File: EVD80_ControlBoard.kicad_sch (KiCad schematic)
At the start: 92 parts, among them U1 LD1117S12TR_SOT223, U2 R-78E3.3-1.0, U3 R-78E5.0-1.0, U4 TL431, U5 LMV324, U7 TMS320F28379DPTPQ

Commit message: Добавления: Расставил все на плате
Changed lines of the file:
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@@
 	)
 	(global_label "VREFHIC"
-		(shape input)
+		(shape output)
 		(at 129.54 250.19 0)
 		(fields_autoplaced yes)
@@
 		)
 		(property "Intersheetrefs" "${INTERSHEET_REFS}"
-			(at 139.7545 250.1106 0)
+			(at 140.3267 250.19 0)
 			(effects
 				(font
@@
 	)
 	(global_label "VREFHID"
-		(shape input)
+		(shape output)
 		(at 193.04 250.19 0)
 		(fields_autoplaced yes)
@@
 		)
 		(property "Intersheetrefs" "${INTERSHEET_REFS}"
-			(at 203.2545 250.1106 0)
+			(at 203.8267 250.19 0)
 			(effects
 				(font
@@
 	)
 	(global_label "VREFHIA"
-		(shape input)
+		(shape output)
 		(at 191.77 212.09 0)
 		(fields_autoplaced yes)
@@
 		)
 		(property "Intersheetrefs" "${INTERSHEET_REFS}"
-			(at 201.8031 212.0106 0)
+			(at 202.3753 212.09 0)
 			(effects
 				(font
@@
 	)
 	(global_label "VREFHIB"
-		(shape input)
+		(shape output)
 		(at 128.27 212.09 0)
 		(fields_autoplaced yes)
@@
 		)
 		(property "Intersheetrefs" "${INTERSHEET_REFS}"
-			(at 138.4845 212.0106 0)
+			(at 139.0567 212.09 0)
 			(effects
 				(font

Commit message: Изменения: развел все
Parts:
- R5: value 1.5k -> 680
- R6: value 1.5k -> 1k
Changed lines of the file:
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@@
 		(fields_autoplaced yes)
 		(property "Reference" "R6"
-			(at 98.298 98.2253 0)
-			(effects
-				(font
-					(size 1.27 1.27)
-				)
-				(justify left)
-			)
-		)
-		(property "Value" "1.5k"
-			(at 98.298 100.7622 0)
+			(at 99.06 97.7899 0)
+			(effects
+				(font
+					(size 1.27 1.27)
+				)
+				(justify left)
+			)
+		)
+		(property "Value" "1k"
+			(at 99.06 100.3299 0)
 			(effects
 				(font
@@
 		(fields_autoplaced yes)
 		(property "Reference" "R5"
-			(at 98.298 47.4253 0)
-			(effects
-				(font
-					(size 1.27 1.27)
-				)
-				(justify left)
-			)
-		)
-		(property "Value" "1.5k"
-			(at 98.298 49.9622 0)
-			(effects
-				(font
+			(at 99.06 46.9899 0)
+			(effects
+				(font
+					(size 1.27 1.27)
+				)
+				(justify left)
+			)
+		)
+		(property "Value" "680"
+			(at 99.06 49.5299 0)
+			(effects
+				(font

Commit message: REV_C: добавил Э3
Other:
- note added: "НВЦТ.EVP150-2-1.3000.100"
- note added: "Схема электрическая принципиальная"
- company: (none) -> ООО "Электротранспортные технологии"
- title: (none) -> Плата управления
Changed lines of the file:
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@@
 (kicad_sch
-	(version 20231120)
+	(version 20250114)
 	(generator "eeschema")
-	(generator_version "8.0")
+	(generator_version "9.0")
 	(paper "A3")
+	(title_block
+		(title "Плата управления")
+		(company "ООО \"Электротранспортные технологии\"")
+		(comment 1 "НВЦТ.EVP150-2-1.3000.100 Э3")
+		(comment 2 "Филатов А.С.")
+		(comment 3 "Сизякин А.В.")
+		(comment 4 "Коваленко В.А.")
+		(comment 6 "Зубков Д.Н.")
+	)
+	(text "Схема электрическая принципиальная"
+		(exclude_from_sim no)
+		(at 330.708 272.288 0)
+		(effects
+			(font
+				(size 2.5 2.5)
+			)
+		)
+	)
+	(text "1.2V Regulator"
+		(exclude_from_sim no)
+		(at 67.31 133.35 0)
+		(effects
+			(font
+				(size 2.543 2.543)
+			)
+			(justify left bottom)
+		)
+	)
+	(text "3.3V Regulator"
+		(exclude_from_sim no)
+		(at 59.69 31.75 0)
+		(effects
+			(font
+				(size 2.543 2.543)
+			)
+			(justify left bottom)
+		)
+	)
+	(text "НВЦТ.EVP150-2-1.3000.100"
+		(exclude_from_sim no)
+		(at 16.51 35.306 90)
+		(effects
+			(font
+				(size 2.5 2.5)
+			)
+		)
+	)
+	(text "5V Regulator"
+		(exclude_from_sim no)
+		(at 59.69 82.55 0)
+		(effects
+			(font
+				(size 2.543 2.543)
+			)
+			(justify left bottom)
+		)
+	)
+	(text "ADC Reference"
+		(exclude_from_sim no)
+		(at 73.66 190.5 0)
+		(effects
+			(font
+				(size 2.543 2.543)
+			)
+			(justify left bottom)
+		)
+	)
+	(text "Hierarchical Sheets"
+		(exclude_from_sim no)
+		(at 490.22 15.24 0)
+		(effects
+			(font
+				(size 5.08 5.08)
+			)
+			(justify left bottom)
+		)
+	)
 	(junction
 		(at 368.3 81.28)
@@
 		)
 	)
-	(text "1.2V Regulator"
-		(exclude_from_sim no)
-		(at 67.31 133.35 0)
-		(effects
-			(font
-				(size 2.543 2.543)
-			)
-			(justify left bottom)
-		)
-	)
-	(text "3.3V Regulator"
-		(exclude_from_sim no)
-		(at 59.69 31.75 0)
-		(effects
-			(font
-				(size 2.543 2.543)
-			)
-			(justify left bottom)
-		)
-	)
-	(text "5V Regulator"
-		(exclude_from_sim no)
-		(at 59.69 82.55 0)
-		(effects
-			(font
-				(size 2.543 2.543)
-			)
-			(justify left bottom)
-		)
-	)
-	(text "ADC Reference"
-		(exclude_from_sim no)
-		(at 73.66 190.5 0)
-		(effects
-			(font
-				(size 2.543 2.543)
-			)
-			(justify left bottom)
-		)
-	)
-	(text "Hierarchical Sheets"
-		(exclude_from_sim no)
-		(at 490.22 15.24 0)
-		(effects
-			(font
-				(size 5.08 5.08)
-			)
-			(justify left bottom)
-		)
-	)
 	(global_label "VREFHIC"
 		(shape output)
@@
 		(at 508 177.8)
 		(size 36.83 25.4)
+		(exclude_from_sim no)
+		(in_bom yes)
+		(on_board yes)
+		(dnp no)
 		(stroke
 			(width 0.1524)
@@
 		(at 558.8 25.4)
 		(size 38.1 25.4)
+		(exclude_from_sim no)
+		(in_bom yes)
+		(on_board yes)
+		(dnp no)
 		(stroke
 			(width 0.1524)
@@
 		(at 558.8 177.8)
 		(size 38.1 25.4)
+		(exclude_from_sim no)
+		(in_bom yes)
+		(on_board yes)
+		(dnp no)
 		(stroke
 			(width 0.1524)
@@
 		(at 508 63.5)
 		(size 38.1 25.4)
+		(exclude_from_sim no)
+		(in_bom yes)
+		(on_board yes)
+		(dnp no)
 		(stroke
 			(width 0.1524)
@@
 		(at 508 139.7)
 		(size 38.1 25.4)
+		(exclude_from_sim no)
+		(in_bom yes)
+		(on_board yes)
+		(dnp no)
 		(stroke
 			(width 0.1524)
@@
 		(at 457.2 25.4)
 		(size 38.1 25.4)
+		(exclude_from_sim no)
+		(in_bom yes)
+		(on_board yes)
+		(dnp no)
 		(stroke
 			(width 0.1524)
@@
 		(at 457.2 177.8)
 		(size 38.1 25.4)
+		(exclude_from_sim no)
+		(in_bom yes)
+		(on_board yes)
+		(dnp no)
 		(stroke
 			(width 0.1524)
@@
 		(at 558.8 101.6)
 		(size 38.1 25.4)
+		(exclude_from_sim no)
+		(in_bom yes)
+		(on_board yes)
+		(dnp no)
 		(stroke
 			(width 0.1524)
@@
 		(at 457.2 139.7)
 		(size 38.1 25.4)
+		(exclude_from_sim no)
+		(in_bom yes)
+		(on_board yes)
+		(dnp no)
 		(stroke
 			(width 0.1524)
@@
 		(at 508 101.6)
 		(size 38.1 25.4)
+		(exclude_from_sim no)
+		(in_bom yes)
+		(on_board yes)
+		(dnp no)
 		(stroke
 			(width 0.1524)
@@
 		(at 457.2 101.6)
 		(size 38.735 25.4)
+		(exclude_from_sim no)
+		(in_bom yes)
+		(on_board yes)
+		(dnp no)
 		(stroke
 			(width 0.1524)
@@
 		(at 508 25.4)
 		(size 38.1 25.4)
+		(exclude_from_sim no)
+		(in_bom yes)
+		(on_board yes)
+		(dnp no)
 		(stroke
 			(width 0.1524)
@@
 		(at 457.2 63.5)
 		(size 38.1 25.4)
+		(exclude_from_sim no)
+		(in_bom yes)
+		(on_board yes)
+		(dnp no)
 		(stroke
 			(width 0.1524)
@@
 		(at 558.8 139.7)
 		(size 38.1 25.4)
+		(exclude_from_sim no)
+		(in_bom yes)
+		(on_board yes)
+		(dnp no)
 		(stroke
 			(width 0.1524)
@@
 		(at 457.2 215.9)
 		(size 38.1 25.4)
+		(exclude_from_sim no)
+		(in_bom yes)
+		(on_board yes)
+		(dnp no)
 		(stroke
 			(width 0.1524)
@@
 		(at 558.8 63.5)
 		(size 38.1 25.4)
+		(exclude_from_sim no)
+		(in_bom yes)
+		(on_board yes)
+		(dnp no)
 		(stroke
 			(width 0.1524)
@@
 		)
 	)
+	(embedded_fonts no)
+	(embedded_files
+		(file
+			(name "gost_landscape.kicad_wks")
+			(type worksheet)
+			(data |KLUv/WC6IO0nAEYqgjFAc9pUwaAq7rGQvf7J+ej28lrFVi+Ra0Qr0XvBpp0PVIKJocju3inLuMxu
+				WJMBZ+8LfABnAHoALNo2GUZx9Wyv+vGO7GqGEQi0h1NBVbQbu4asUlxtNdu0DUOHHXuz3S4LorjC
+				2E01EGgMV8+VUWw3dfNo1moMH81SFXzgYBtVTc4wznZ5FqxD7VTQq7ccP9gGTKJmWIeqoOVcJzCQ
+				DVVL8SfCVhDFDBBgIzTR1VmonOtDBRi2oWoZrJTd7jX9n7Khe3Oye/9Ms1rmYPfHZufeRc3LSf+n
+				jA0dvmaRc3bwZWv+XePfzun8KCGM/7Cfewzne/kzOnz97xpCdtQnfM1OdoRSwyL6ns9/yCEXdTKt
+				OdMw+9FeW47UoQcp1/Kgs+ReeFeQbod89jhy6K+b4b9sl8309ehUweEadu1UTChOpuuy4U1LLpJO
+				lVtSuhJakbPaCV0eintGDej97uhEuhmOcrWX1TbJb5lclmu6pItyMa5v1WZ1wyIHzIIiICx/hlaE
+				zSDtgyDQGGvlWpxSbsstXdJLQQAB1cP21+/uObTaZWza0c22HZYs36ROMpS0m+FjF6MbeD2fZOgw
+				wZ3rg/x/m2kOFM+HkHnw/SDTPLsg89wrZHil5ZLQ0Wmkp4vQlk4KkREFxB1+PPn90ttfe+myyeUD
+				umO5J3flmlwuU5xO7sejFKfRiSWBbahBUahmpCAFSSHDGnGRwBiC1Z0dskgQgjAUw4AcCGIcAhlC
+				HCFEQAwhhBhjREauHS1W9GqoT2ej9oib6AkUZ1xytemsseM0xpmg8F4VpZ0BeQEinRqXR/LHvcXM
+				zxBtuIUaw8HcSNawPE002iKV23H6UV273ntSIAlTA5N1ZdrndCiVe6uBaRiHYYiKq9GgNrTeNTRf
+				NfUJ/32bWh9/57DHw7uQxz4ULHfFeApmWDLvyo3GHRcRbczSKYx08fXGVh6xzSXRvDpB6BApYY8y
+				6sEbrKBGeegRkrjMrCrrLxeLYxp0HswTCskvDBMXTHE/T+ByeqaPP3qdKzND8/1VD3bUDeJn0Y9z
+				gDZPfEvFjAaAJZpbLUtz3kaxhDe3Snk/4OyFwqFNmJyv7iYuCzQrtB3ykyQKiwBJcw2JxNU32g3/
+				kVAxeFgRdQg12uIi1pyRGPpIH4Xa+rlwJouAD+8zrEHs/Mj95yRfSbzxr/d0A4lRg1eZtAqJQBlT
+				3zHGdrqzkPo5zEAHci6R5WaJ7M8aOMeYTH8ylU/JOjqDbeYB3A/SED8iC0uFsZZlGFxjlGVAmFBW
+				Sg295mriH68MGT6sxAPRzPNjscyiXi6CHelA4On6CGhR0TBQg6X1agUnjA2o+EQ8+EMjOt0EE3O1
+				KZXjk96NgCgPyIEYPya3WbCT53yDvYomiSBeq3cTdXyh8ErjMLtLd9lDpdvsZ53W2mh1ArZ1o9W/
+				pn4MvGAJn4RflojuA5iT3WAhYm7x+ywpKbA6SP8AsvhaPKoyXAVabGD5KqtYRIZHh+1qjSosK7Zk
+				WnUXr26KKLGZ9FmofbXdLWEkLIYWnz6CoHAJ1aETYyMLDNADH7/BUkuXmDcZVyKv/jweRknOlknx
+				InFQ+uGQOpYGNF5vgyfg9IZKup03LTR7DEu7ADGKQmGCR30jTPWNMAURYVmFlx3OQiIuT/p0NIV4
+				k5jbGQYYpblIqpu8oZ6A0nlGAufJ/aGmRk8NeaaILFcB|
+			)
+			(checksum "9180C2D8C133E7F089AA5E43F4962E04")
+		)
+	)

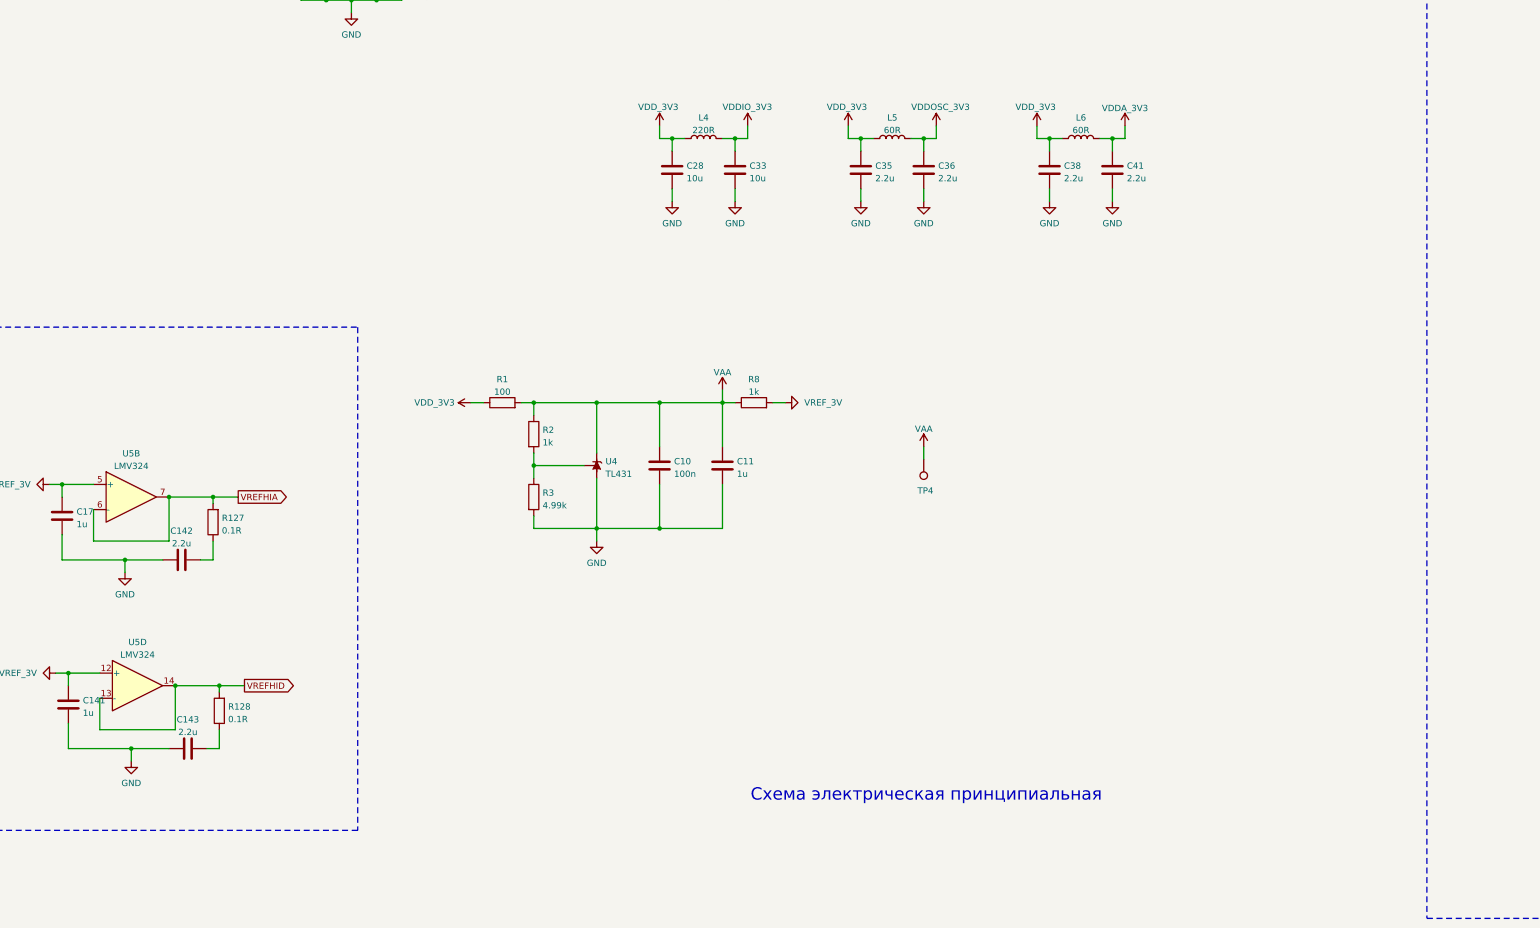
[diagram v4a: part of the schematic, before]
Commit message: REV_C: исправил Э3 и СБ
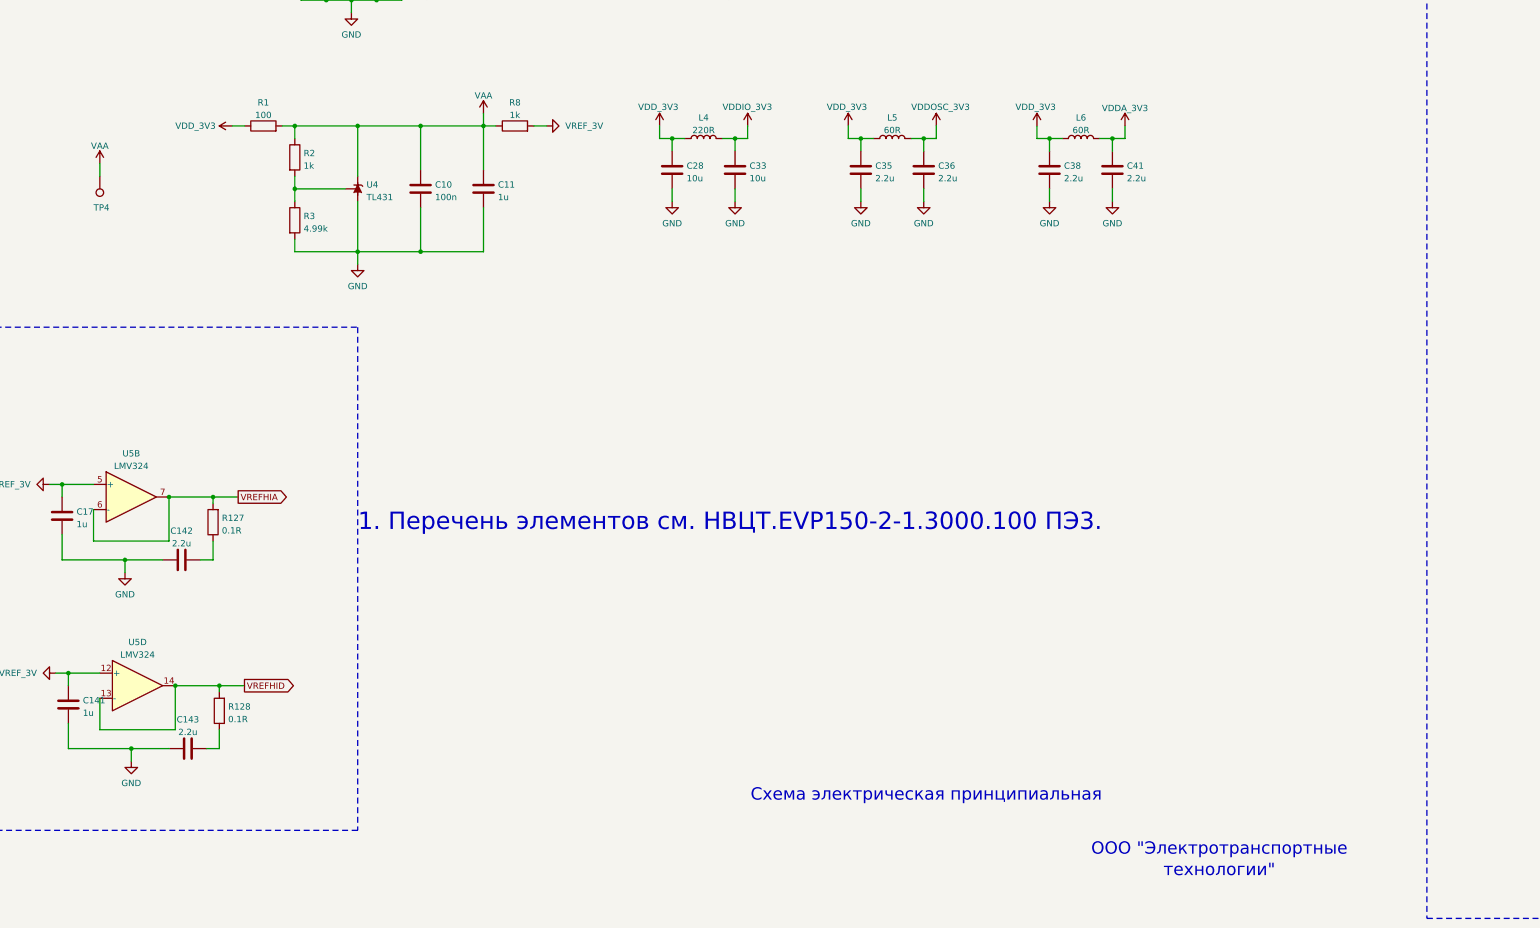
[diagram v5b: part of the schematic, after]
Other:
- note added: "1. Перечень элементов см. НВЦТ.EVP150-2-1.3000.100 ПЭ3."
- note added: "ООО "Электротранспортные"
- note added: "технологии""
- company: ООО "Электротранспортные технологии" -> (none)
- moved on the sheet: C10, C11, R1, R2, R3, R8, TP4, U4
